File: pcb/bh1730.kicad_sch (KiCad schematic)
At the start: 7 parts, among them J3 I2C Board, J4 I2C Sensor, U2 BH1730FVC

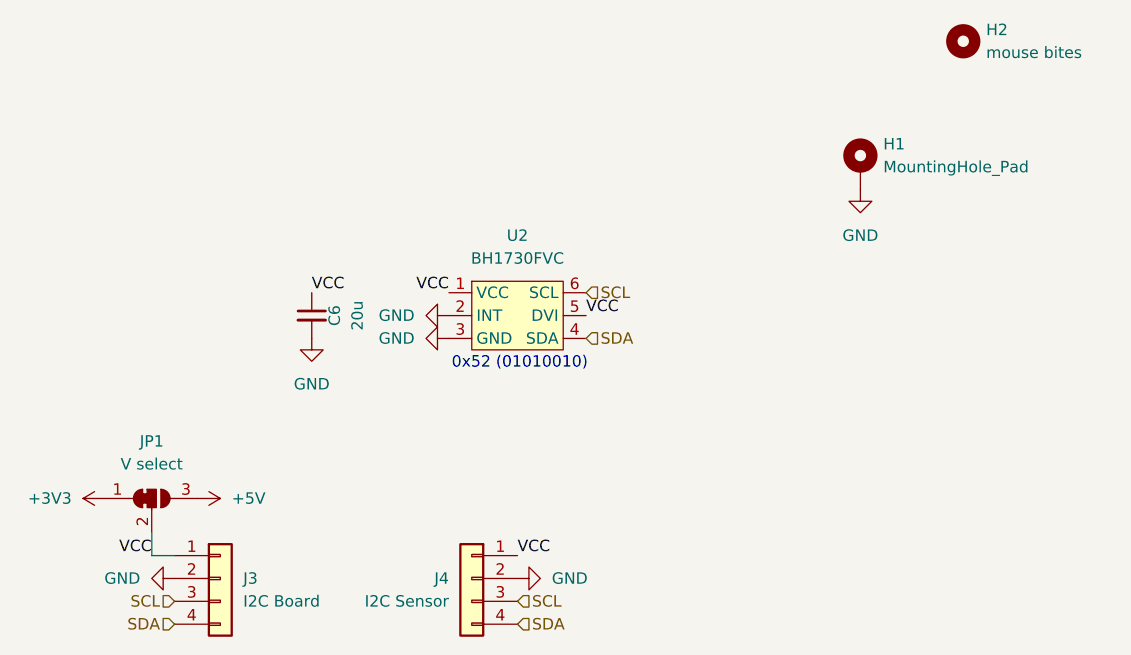
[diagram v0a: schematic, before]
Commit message: Rename pcb, add sensors and fix some issues
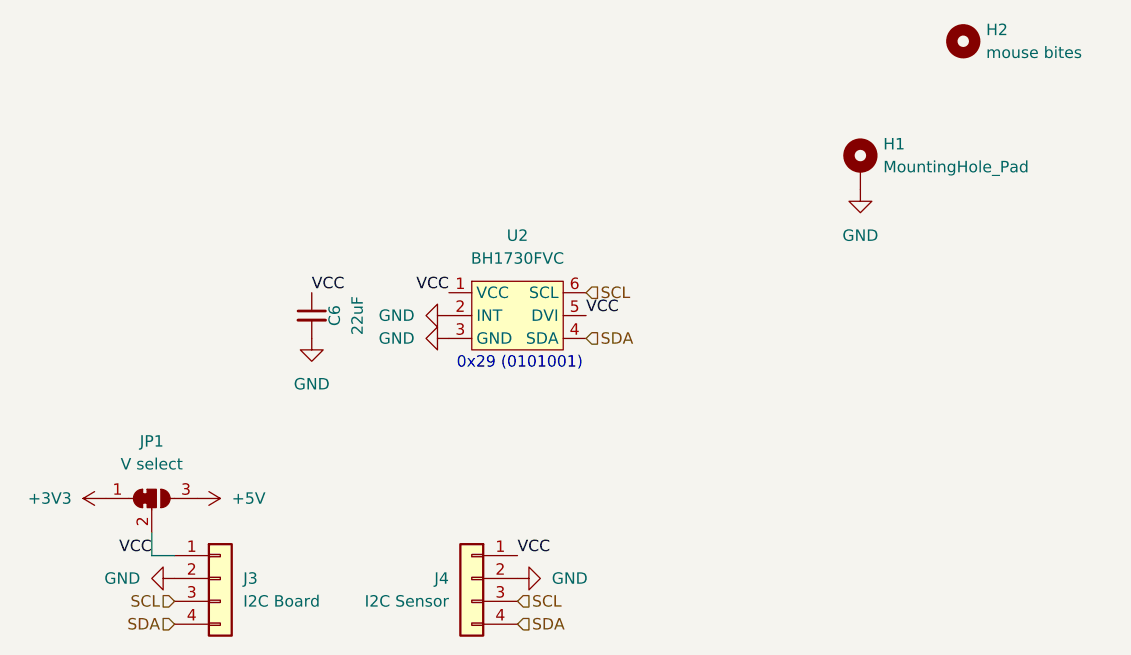
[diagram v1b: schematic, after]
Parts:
- C6: value 20u -> 22uF
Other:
- note added: "0x29 (0101001)"
- note removed: "0x52 (01010010)"
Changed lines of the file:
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@@
 		)
 	)
-	(text "0x52 (01010010)"
+	(text "0x29 (0101001)"
 		(exclude_from_sim no)
 		(at 77.724 80.264 0)
@@
 			)
 		)
-		(property "Value" "20u"
+		(property "Value" "22uF"
 			(at 59.69 74.93 90)
 			(effects
